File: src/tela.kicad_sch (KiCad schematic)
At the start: 14 parts, among them Q3 Q_NMOS_SGD, Q4 Q_NMOS_SGD

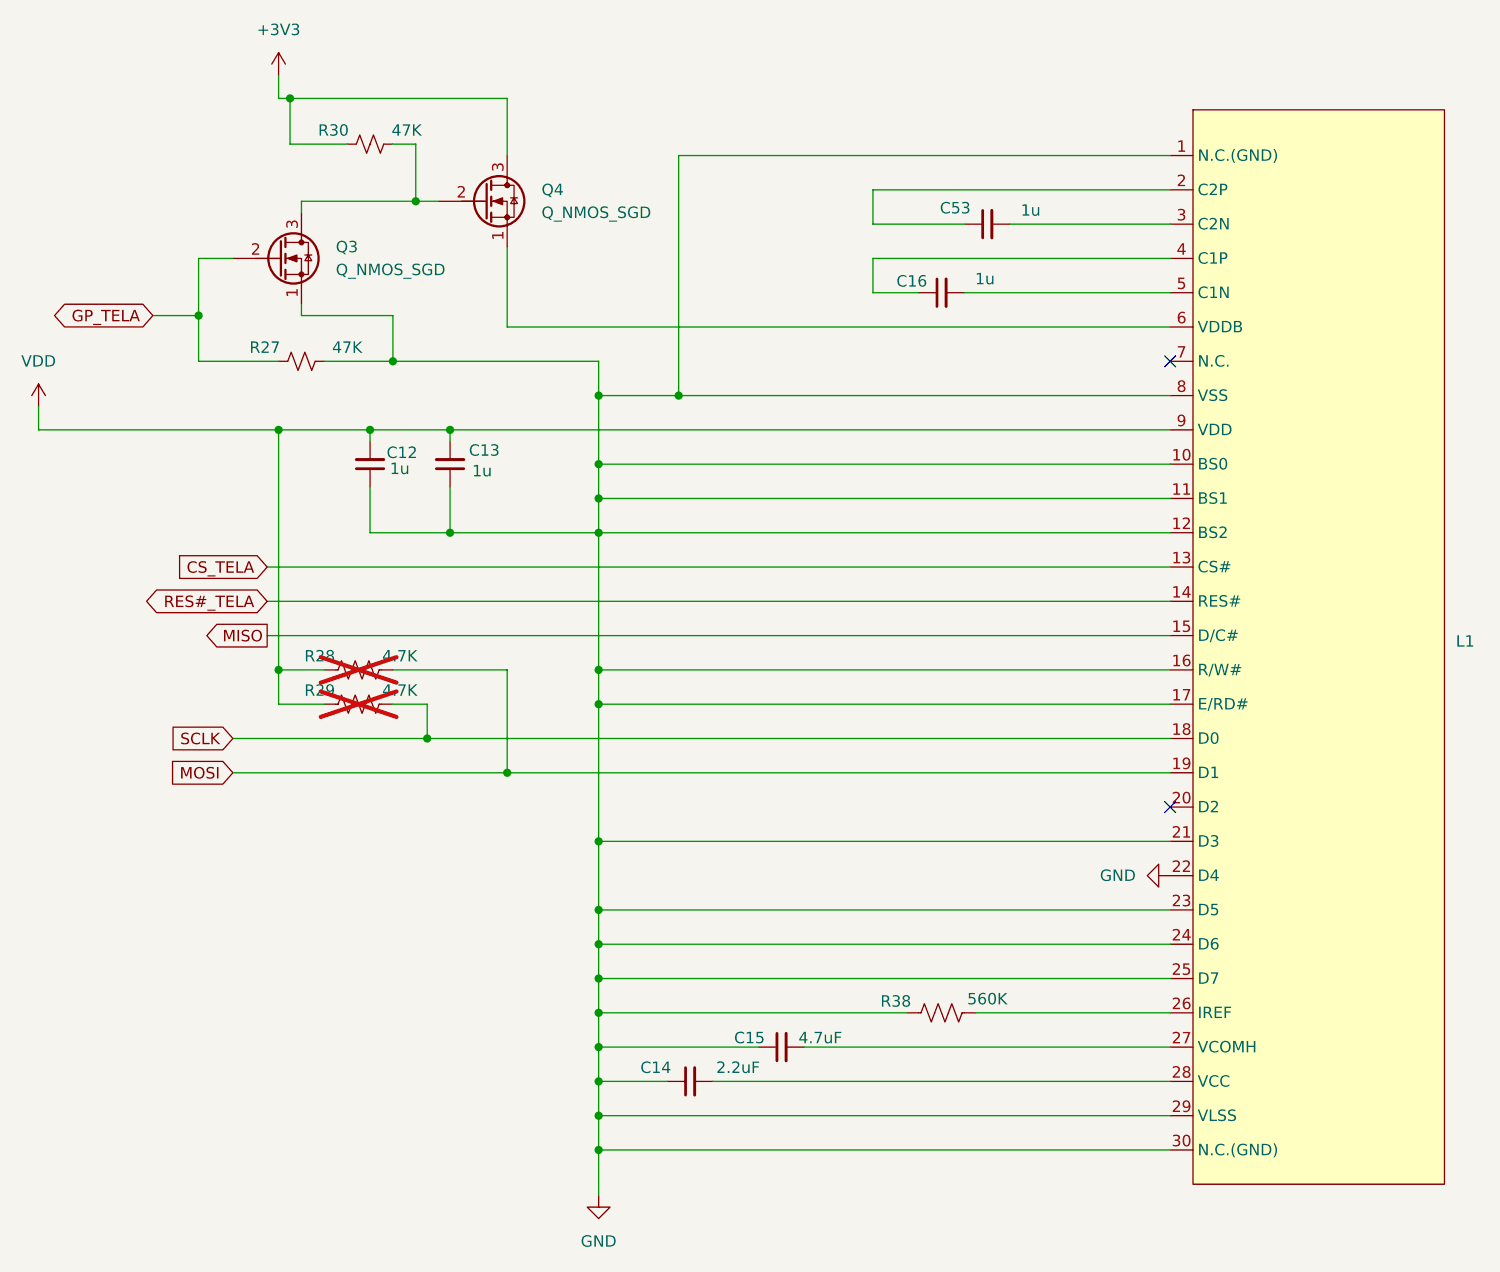
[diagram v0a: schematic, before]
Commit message: fix: Consertando paginação e refact da Tela_OLED
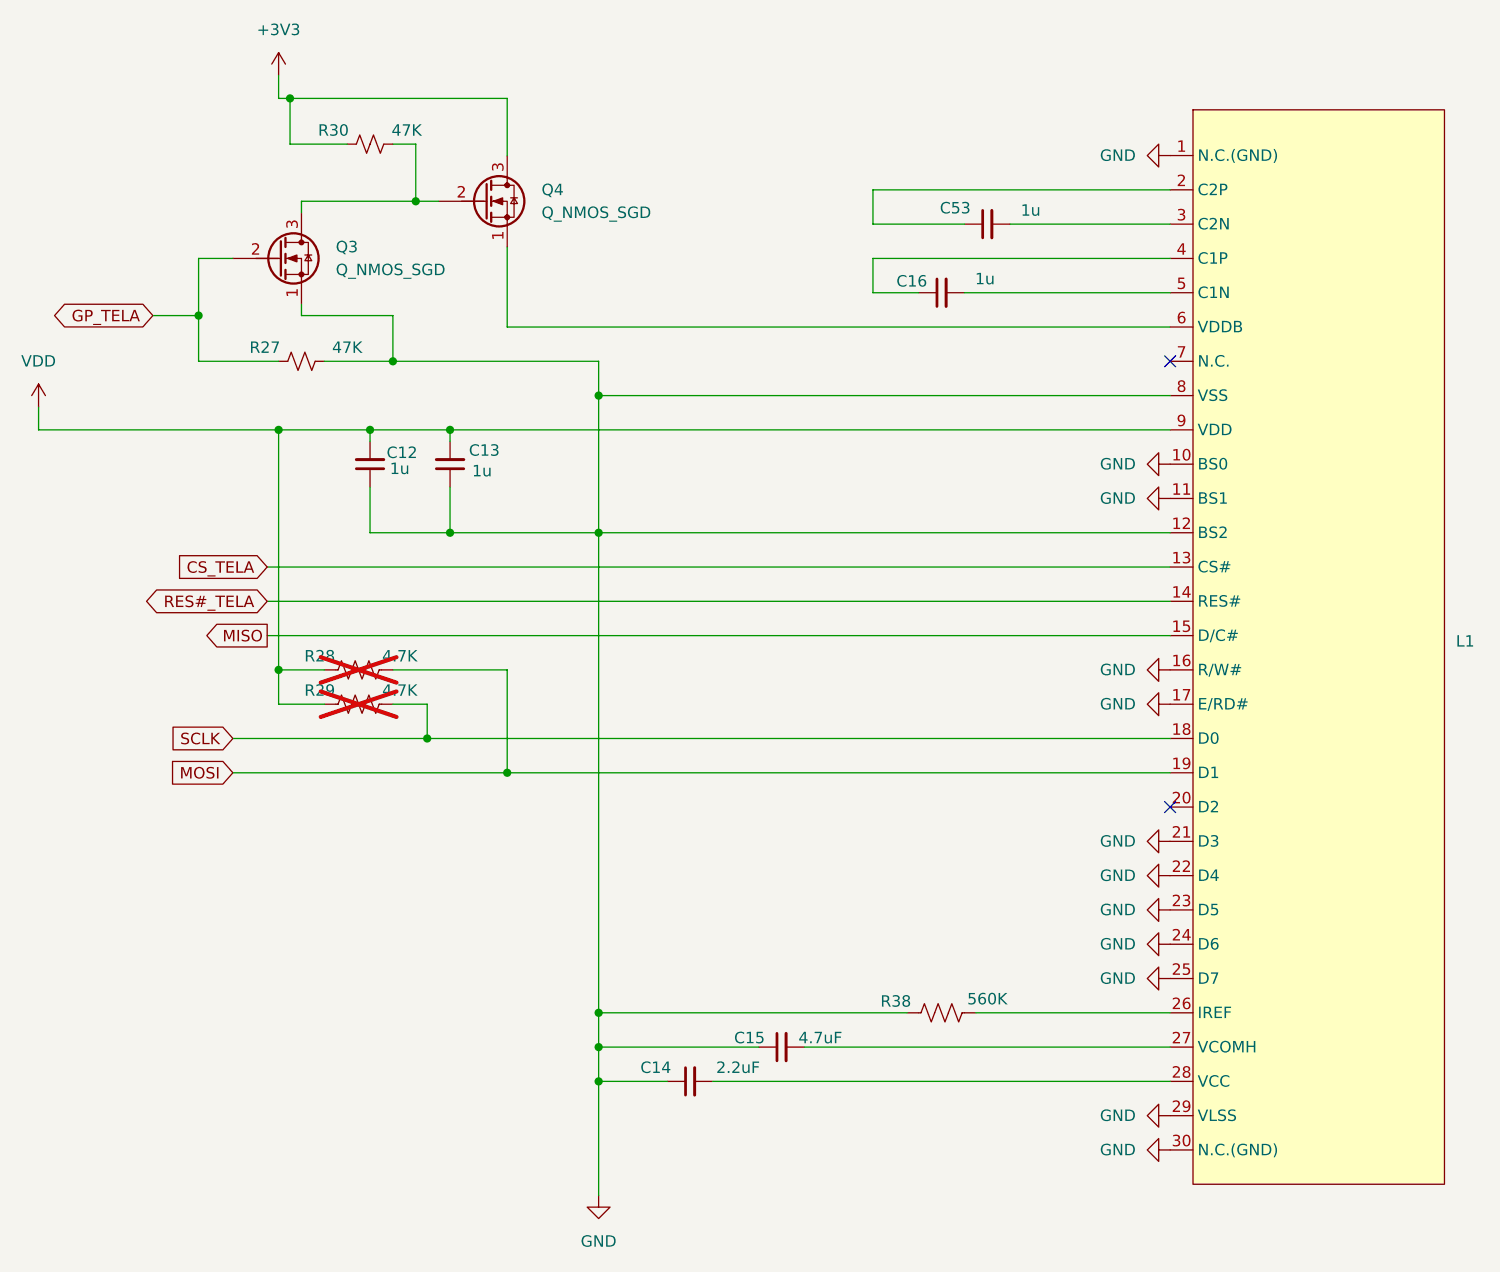
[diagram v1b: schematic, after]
